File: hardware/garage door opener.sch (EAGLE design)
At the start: 26 parts, among them K1 HE3621, K2 HE3621

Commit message: Updated with BOM
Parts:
- C1, C2: value (none) -> 10uf
- D1, D2: value (none) -> 1N4004
- OPEN1, OPEN2, SENS1, SENS2: MPN (none) -> OSTTE020161
- R1, R3: value (none) -> 20
- R2, R4: value 2.3k -> 4k
- R5, R6: value (none) -> 1k
- T1, T2: MPN (none) -> MMBT2222A
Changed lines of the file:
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@@
 </classes>
 <parts>
-<part name="T1" library="transistor-neu-to92" deviceset="*-NPN-" device="SOT23-BEC" technology="MMBT3904LT1"/>
+<part name="T1" library="transistor-neu-to92" deviceset="*-NPN-" device="SOT23-BEC" technology="MMBT3904LT1">
+<attribute name="MPN" value="MMBT2222A"/>
+</part>
 <part name="K1" library="relay" deviceset="HE3621" device="">
 <attribute name="MPN" value="HE3621A0510"/>
@@
 <part name="JP2" library="pinhead" deviceset="PINHD-1X15" device=""/>
 <part name="JP3" library="pinhead" deviceset="PINHD-1X15" device=""/>
-<part name="OPEN1" library="adafruit" deviceset="1X2" device="-3.5MM"/>
-<part name="SENS1" library="adafruit" deviceset="1X2" device="-3.5MM"/>
+<part name="OPEN1" library="adafruit" deviceset="1X2" device="-3.5MM">
+<attribute name="MPN" value="OSTTE020161"/>
+</part>
+<part name="SENS1" library="adafruit" deviceset="1X2" device="-3.5MM">
+<attribute name="MPN" value="OSTTE020161"/>
+</part>
 <part name="+3V1" library="supply1" deviceset="+3V3" device=""/>
 <part name="P+1" library="supply1" deviceset="+5V" device=""/>
 <part name="GND1" library="supply1" deviceset="GND" device=""/>
-<part name="R1" library="resistor" deviceset="R-US_" device="R0603"/>
+<part name="R1" library="resistor" deviceset="R-US_" device="R0603" value="20"/>
 <part name="+3V2" library="supply1" deviceset="+3V3" device=""/>
 <part name="P+2" library="supply1" deviceset="+5V" device=""/>
 <part name="GND2" library="supply1" deviceset="GND" device=""/>
-<part name="R2" library="resistor" deviceset="R-US_" device="R0603" value="2.3k"/>
-<part name="D1" library="diode" deviceset="DIODE-" device="DO214BA"/>
-<part name="C1" library="resistor" deviceset="C-US" device="C0603"/>
-<part name="C2" library="resistor" deviceset="C-US" device="C0603"/>
+<part name="R2" library="resistor" deviceset="R-US_" device="R0603" value="4k"/>
+<part name="D1" library="diode" deviceset="DIODE-" device="DO214BA" value="1N4004"/>
+<part name="C1" library="resistor" deviceset="C-US" device="C0603" value="10uf"/>
+<part name="C2" library="resistor" deviceset="C-US" device="C0603" value="10uf"/>
 <part name="P+3" library="supply1" deviceset="+5V" device=""/>
 <part name="+3V3" library="supply1" deviceset="+3V3" device=""/>
@@
 <part name="LED1" library="resistor" deviceset="R-US_" device="R0603"/>
 <part name="LED2" library="resistor" deviceset="R-US_" device="R0603"/>
-<part name="SENS2" library="adafruit" deviceset="1X2" device="-3.5MM"/>
-<part name="R3" library="resistor" deviceset="R-US_" device="R0603"/>
+<part name="SENS2" library="adafruit" deviceset="1X2" device="-3.5MM">
+<attribute name="MPN" value="OSTTE020161"/>
+</part>
+<part name="R3" library="resistor" deviceset="R-US_" device="R0603" value="20"/>
 <part name="+3V4" library="supply1" deviceset="+3V3" device=""/>
 <part name="K2" library="relay" deviceset="HE3621" device="">
 <attribute name="MPN" value="HE3621A0510"/>
 </part>
-<part name="OPEN2" library="adafruit" deviceset="1X2" device="-3.5MM"/>
-<part name="T2" library="transistor-neu-to92" deviceset="*-NPN-" device="SOT23-BEC" technology="MMBT3904LT1"/>
+<part name="OPEN2" library="adafruit" deviceset="1X2" device="-3.5MM">
+<attribute name="MPN" value="OSTTE020161"/>
+</part>
+<part name="T2" library="transistor-neu-to92" deviceset="*-NPN-" device="SOT23-BEC" technology="MMBT3904LT1">
+<attribute name="MPN" value="MMBT2222A"/>
+</part>
 <part name="P+4" library="supply1" deviceset="+5V" device=""/>
-<part name="D2" library="diode" deviceset="DIODE-" device="DO214BA"/>
-<part name="R4" library="resistor" deviceset="R-US_" device="R0603" value="2.3k"/>
+<part name="D2" library="diode" deviceset="DIODE-" device="DO214BA" value="1N4004"/>
+<part name="R4" library="resistor" deviceset="R-US_" device="R0603" value="4k"/>
 <part name="GND5" library="supply1" deviceset="GND" device=""/>
 <part name="JP4" library="pinhead" deviceset="PINHD-1X3" device=""/>
 <part name="D3" library="diode" deviceset="1N4004" device=""/>
 <part name="D4" library="diode" deviceset="1N4004" device=""/>
-<part name="R5" library="resistor" deviceset="R-US_" device="R0603"/>
-<part name="R6" library="resistor" deviceset="R-US_" device="R0603"/>
+<part name="R5" library="resistor" deviceset="R-US_" device="R0603" value="1k"/>
+<part name="R6" library="resistor" deviceset="R-US_" device="R0603" value="1k"/>
 </parts>
 <sheets>
@@
 </plain>
 <instances>
-<instance part="T1" gate="G$1" x="149.86" y="101.6"/>
+<instance part="T1" gate="G$1" x="149.86" y="101.6">
+<attribute name="MPN" x="149.86" y="101.6" size="1.778" layer="96" display="off"/>
+</instance>
 <instance part="K1" gate="1" x="152.4" y="114.3"/>
 <instance part="K1" gate="2" x="165.1" y="114.3"/>
@@
 <instance part="JP2" gate="A" x="68.58" y="38.1"/>
 <instance part="JP3" gate="A" x="119.38" y="38.1"/>
-<instance part="OPEN1" gate="G$1" x="180.34" y="114.3"/>
-<instance part="SENS1" gate="G$1" x="180.34" y="38.1"/>
+<instance part="OPEN1" gate="G$1" x="180.34" y="114.3">
+<attribute name="MPN" x="180.34" y="114.3" size="1.778" layer="96" display="off"/>
+</instance>
+<instance part="SENS1" gate="G$1" x="180.34" y="38.1">
+<attribute name="MPN" x="180.34" y="38.1" size="1.778" layer="96" display="off"/>
+</instance>
 <instance part="+3V1" gate="G$1" x="111.76" y="68.58"/>
 <instance part="P+1" gate="1" x="71.12" y="68.58"/>
@@
 <instance part="LED1" gate="G$1" x="78.74" y="43.18" rot="R90"/>
 <instance part="LED2" gate="G$1" x="83.82" y="38.1" rot="R90"/>
-<instance part="SENS2" gate="G$1" x="180.34" y="25.4"/>
+<instance part="SENS2" gate="G$1" x="180.34" y="25.4">
+<attribute name="MPN" x="180.34" y="25.4" size="1.778" layer="96" display="off"/>
+</instance>
 <instance part="R3" gate="G$1" x="165.1" y="27.94"/>
 <instance part="+3V4" gate="G$1" x="157.48" y="33.02"/>
 <instance part="K2" gate="1" x="152.4" y="76.2"/>
 <instance part="K2" gate="2" x="167.64" y="76.2"/>
-<instance part="OPEN2" gate="G$1" x="180.34" y="76.2"/>
-<instance part="T2" gate="G$1" x="149.86" y="63.5"/>
+<instance part="OPEN2" gate="G$1" x="180.34" y="76.2">
+<attribute name="MPN" x="180.34" y="76.2" size="1.778" layer="96" display="off"/>
+</instance>
+<instance part="T2" gate="G$1" x="149.86" y="63.5">
+<attribute name="MPN" x="149.86" y="63.5" size="1.778" layer="96" display="off"/>
+</instance>
 <instance part="P+4" gate="1" x="152.4" y="88.9"/>
 <instance part="D2" gate="G$1" x="142.24" y="76.2" rot="R90"/>

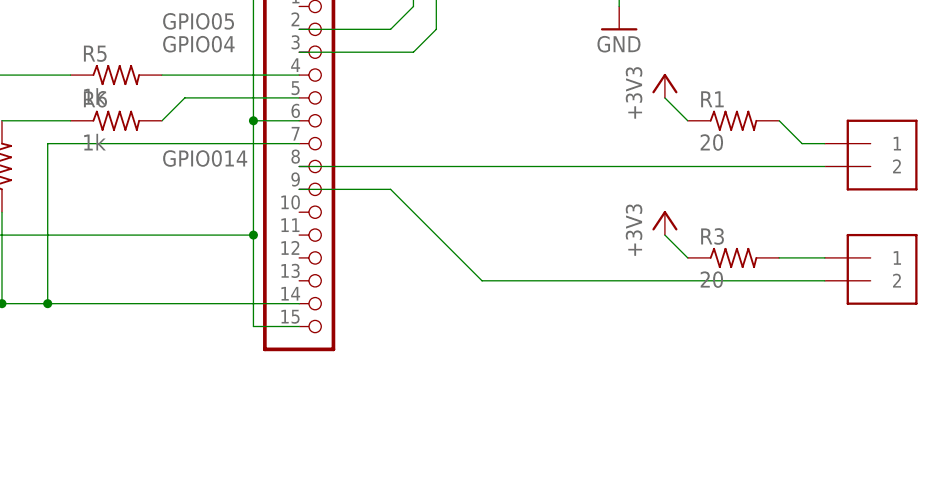
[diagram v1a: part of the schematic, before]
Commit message: Updated with pull down resistor for sense inputs.
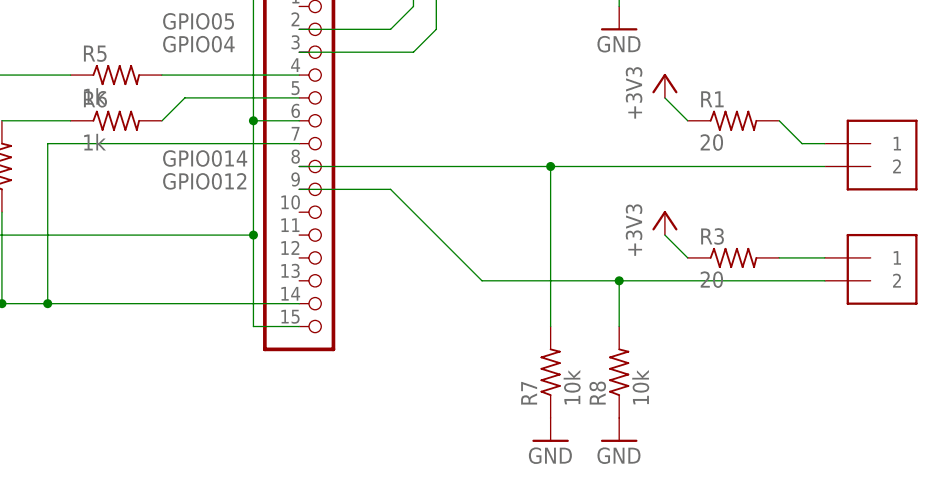
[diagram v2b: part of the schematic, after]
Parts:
- added R7, R8: 10k, resistor:R-US_R0603
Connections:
- net GND: now also R7.1, R8.1
- net N$14: now also R7.2
- net N$22: now also R8.2
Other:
- note added: "GPIO012"
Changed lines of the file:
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@@
 <setting verticaltext="up"/>
 </settings>
-<grid distance="0.1" unitdist="inch" unit="inch" style="lines" multiple="1" display="yes" altdistance="0.01" altunitdist="inch" altunit="inch"/>
+<grid distance="0.1" unitdist="inch" unit="inch" style="lines" multiple="1" display="no" altdistance="0.01" altunitdist="inch" altunit="inch"/>
 <layers>
 <layer number="1" name="Top" color="4" fill="1" visible="no" active="no"/>
@@
 <part name="R5" library="resistor" deviceset="R-US_" device="R0603" value="1k"/>
 <part name="R6" library="resistor" deviceset="R-US_" device="R0603" value="1k"/>
+<part name="R7" library="resistor" deviceset="R-US_" device="R0603" value="10k"/>
+<part name="R8" library="resistor" deviceset="R-US_" device="R0603" value="10k"/>
+<part name="GND6" library="supply1" deviceset="GND" device=""/>
+<part name="GND7" library="supply1" deviceset="GND" device=""/>
 </parts>
 <sheets>
@@
 <text x="101.6" y="50.8" size="1.778" layer="95">GPIO04</text>
 <text x="101.6" y="38.1" size="1.778" layer="95">GPIO014</text>
+<text x="101.6" y="35.56" size="1.778" layer="95">GPIO012</text>
 </plain>
 <instances>
@@
 <instance part="R5" gate="G$1" x="96.52" y="48.26"/>
 <instance part="R6" gate="G$1" x="96.52" y="43.18"/>
+<instance part="R7" gate="G$1" x="144.78" y="15.24" rot="R90"/>
+<instance part="R8" gate="G$1" x="152.4" y="15.24" rot="R90"/>
+<instance part="GND6" gate="1" x="152.4" y="7.62"/>
+<instance part="GND7" gate="1" x="144.78" y="7.62"/>
 </instances>
 <busses>
@@
 <wire x1="152.4" y1="58.42" x2="152.4" y2="55.88" width="0.1524" layer="91"/>
 </segment>
+<segment>
+<pinref part="R8" gate="G$1" pin="1"/>
+<pinref part="GND6" gate="1" pin="GND"/>
+</segment>
+<segment>
+<pinref part="R7" gate="G$1" pin="1"/>
+<pinref part="GND7" gate="1" pin="GND"/>
+</segment>
 </net>
 <net name="+3V3" class="0">
@@
 <segment>
 <pinref part="SENS2" gate="G$1" pin="2"/>
-<wire x1="137.16" y1="25.4" x2="175.26" y2="25.4" width="0.1524" layer="91"/>
+<wire x1="137.16" y1="25.4" x2="152.4" y2="25.4" width="0.1524" layer="91"/>
 <pinref part="JP3" gate="A" pin="9"/>
+<wire x1="152.4" y1="25.4" x2="175.26" y2="25.4" width="0.1524" layer="91"/>
 <wire x1="137.16" y1="25.4" x2="127" y2="35.56" width="0.1524" layer="91"/>
 <wire x1="127" y1="35.56" x2="116.84" y2="35.56" width="0.1524" layer="91"/>
+<pinref part="R8" gate="G$1" pin="2"/>
+<wire x1="152.4" y1="20.32" x2="152.4" y2="25.4" width="0.1524" layer="91"/>
+<junction x="152.4" y="25.4"/>
 </segment>
 </net>
@@
 <pinref part="SENS1" gate="G$1" pin="2"/>
 <pinref part="JP3" gate="A" pin="8"/>
-<wire x1="175.26" y1="38.1" x2="116.84" y2="38.1" width="0.1524" layer="91"/>
-</segment>
-</net>
+<wire x1="175.26" y1="38.1" x2="144.78" y2="38.1" width="0.1524" layer="91"/>
+<pinref part="R7" gate="G$1" pin="2"/>
+<wire x1="144.78" y1="38.1" x2="116.84" y2="38.1" width="0.1524" layer="91"/>
+<wire x1="144.78" y1="20.32" x2="144.78" y2="38.1" width="0.1524" layer="91"/>
+<junction x="144.78" y="38.1"/>
+</segment>
+</net>

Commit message: Lots of refactoring
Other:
- note added: "+3V3 GND +5V"
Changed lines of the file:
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@@
 <text x="101.6" y="38.1" size="1.778" layer="95">GPIO014</text>
 <text x="101.6" y="35.56" size="1.778" layer="95">GPIO012</text>
+<text x="22.86" y="20.32" size="1.778" layer="97">+3V3
+GND
++5V</text>
 </plain>
 <instances>
@@
 </schematic>
 </drawing>
+<compatibility>
+<note version="6.3" minversion="6.2.2" severity="warning">
+Since Version 6.2.2 text objects can contain more than one line,
+which will not be processed correctly with this version.
+</note>
+</compatibility>
 </eagle>

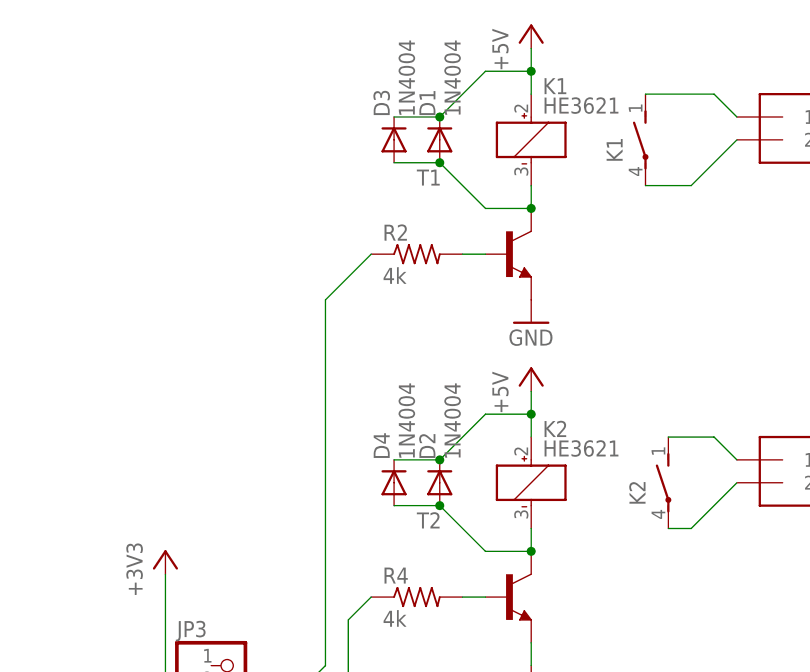
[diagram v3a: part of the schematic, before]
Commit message: Removed trough hole diode, removed top silkscreen, rerouted.
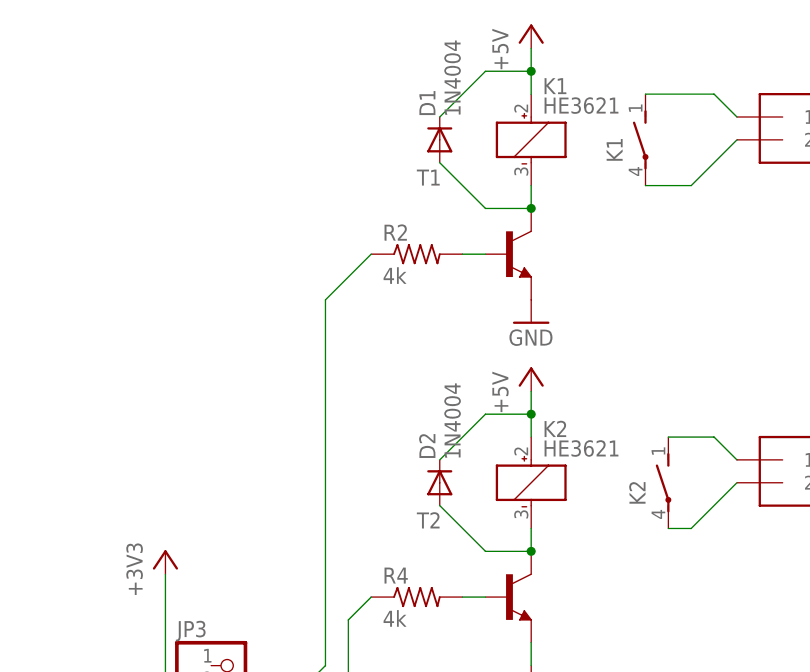
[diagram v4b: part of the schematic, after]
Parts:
- removed D3, D4: 1N4004, diode:1N4004
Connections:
- net +5V: no longer D3.C, D4.C
- net N$16: no longer D3.A
- net N$25: no longer D4.A
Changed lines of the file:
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@@
 <part name="GND5" library="supply1" deviceset="GND" device=""/>
 <part name="JP4" library="pinhead" deviceset="PINHD-1X3" device=""/>
-<part name="D3" library="diode" deviceset="1N4004" device=""/>
-<part name="D4" library="diode" deviceset="1N4004" device=""/>
 <part name="R5" library="resistor" deviceset="R-US_" device="R0603" value="1k"/>
 <part name="R6" library="resistor" deviceset="R-US_" device="R0603" value="1k"/>
@@
 <instance part="GND5" gate="1" x="152.4" y="53.34"/>
 <instance part="JP4" gate="A" x="35.56" y="22.86"/>
-<instance part="D3" gate="1" x="137.16" y="114.3" rot="R90"/>
-<instance part="D4" gate="1" x="137.16" y="76.2" rot="R90"/>
 <instance part="R5" gate="G$1" x="96.52" y="48.26"/>
 <instance part="R6" gate="G$1" x="96.52" y="43.18"/>
@@
 <junction x="152.4" y="121.92"/>
 <pinref part="D1" gate="G$1" pin="C"/>
-<pinref part="D3" gate="1" pin="C"/>
-<wire x1="142.24" y1="116.84" x2="137.16" y2="116.84" width="0.1524" layer="91"/>
-<junction x="142.24" y="116.84"/>
 </segment>
 <segment>
@@
 <wire x1="147.32" y1="83.82" x2="152.4" y2="83.82" width="0.1524" layer="91"/>
 <junction x="152.4" y="83.82"/>
-<pinref part="D4" gate="1" pin="C"/>
-<wire x1="142.24" y1="78.74" x2="137.16" y2="78.74" width="0.1524" layer="91"/>
-<junction x="142.24" y="78.74"/>
 </segment>
 </net>
@@
 <junction x="152.4" y="106.68"/>
 <pinref part="D1" gate="G$1" pin="A"/>
-<pinref part="D3" gate="1" pin="A"/>
-<wire x1="137.16" y1="111.76" x2="142.24" y2="111.76" width="0.1524" layer="91"/>
-<junction x="142.24" y="111.76"/>
 </segment>
 </net>
@@
 <wire x1="147.32" y1="68.58" x2="152.4" y2="68.58" width="0.1524" layer="91"/>
 <junction x="152.4" y="68.58"/>
-<pinref part="D4" gate="1" pin="A"/>
-<wire x1="137.16" y1="73.66" x2="142.24" y2="73.66" width="0.1524" layer="91"/>
-<junction x="142.24" y="73.66"/>
-</segment>
-</net>
+</segment>
+</net>
